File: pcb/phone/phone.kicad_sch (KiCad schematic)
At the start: 27 parts, among them CN1 S2B-PH-SM4-TB, U4 TPS63021DSJR, U5 TPS7A0218PDBVR, U6 MCP73831-2ACI/MC, U7 MAX17048G+T10

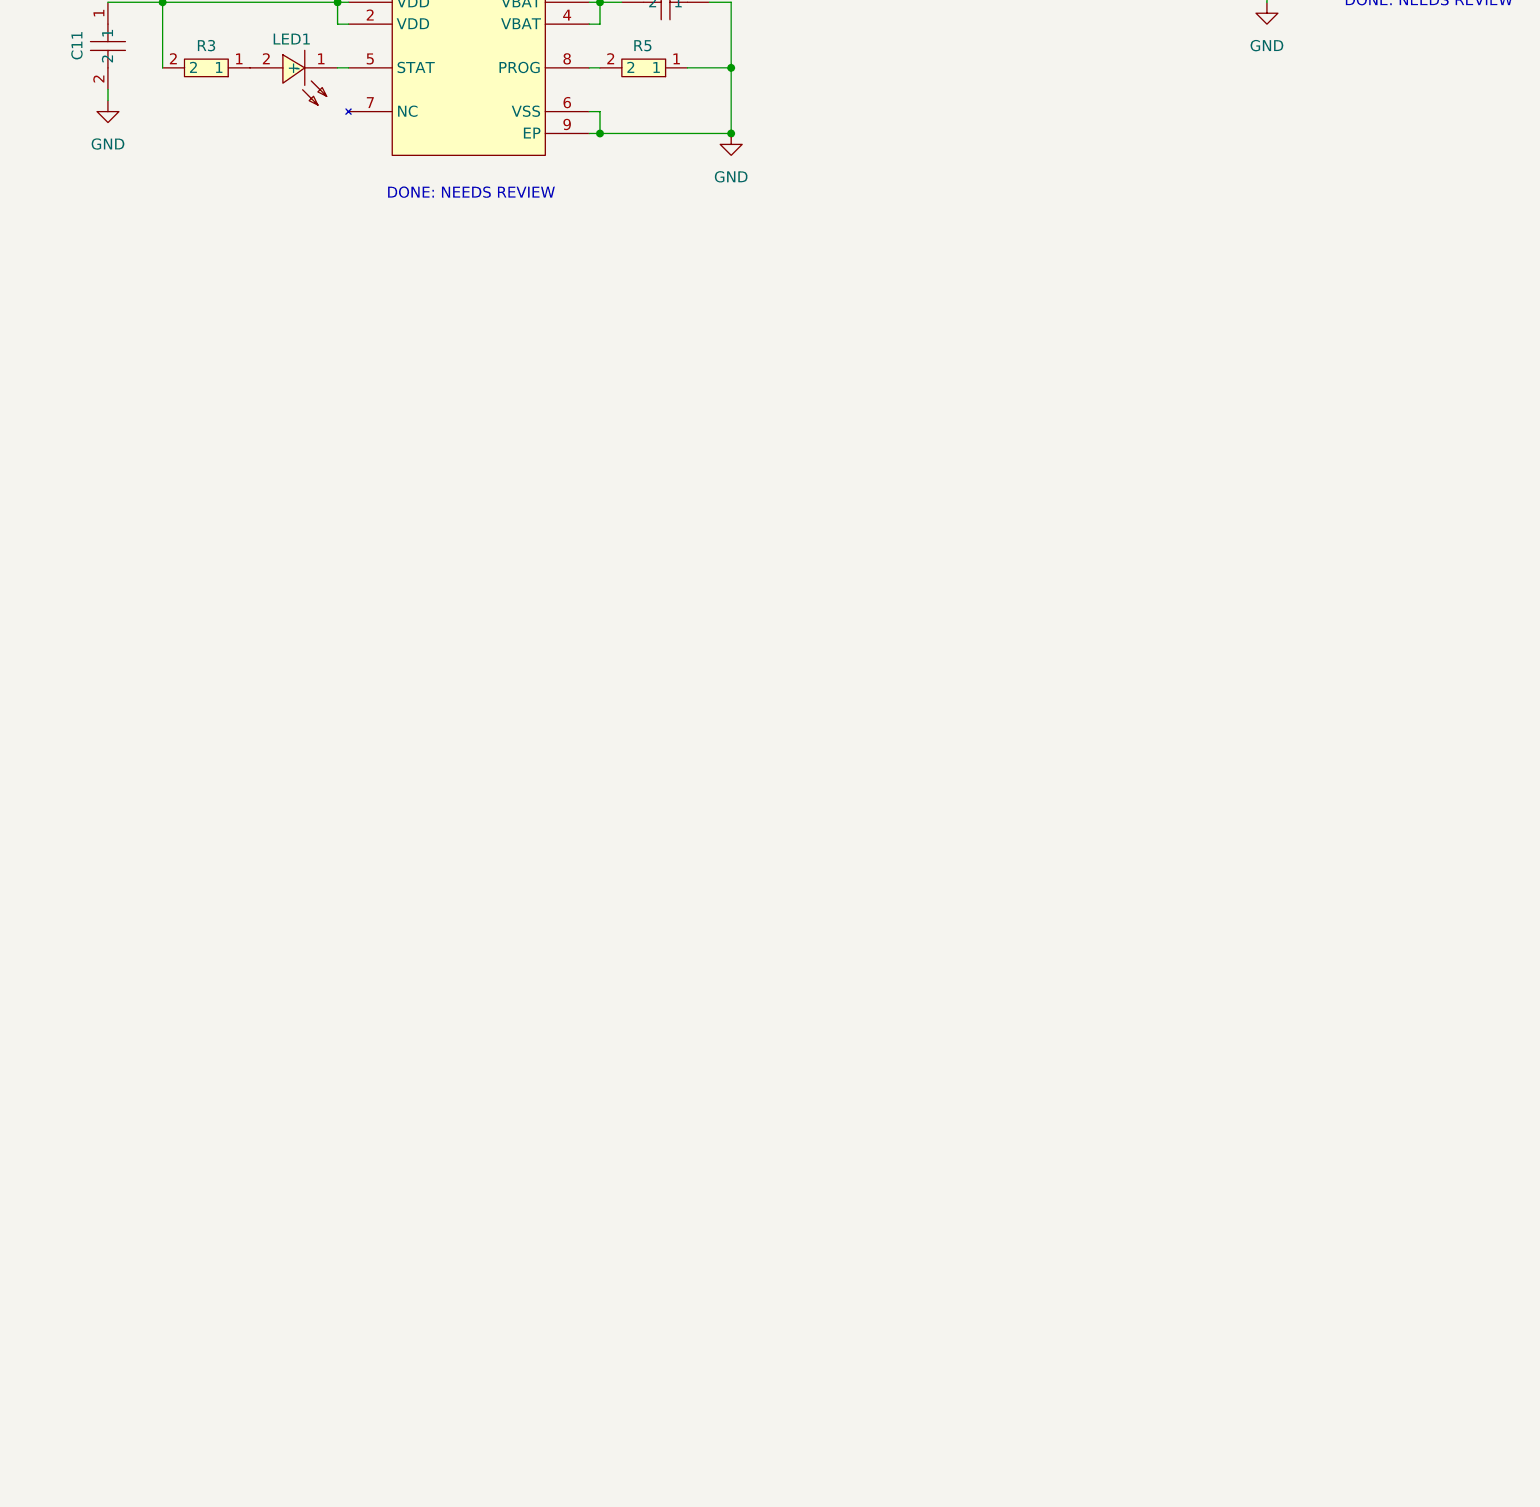
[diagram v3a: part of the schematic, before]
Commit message: Phase 3.2: Add MCU section (STM32H743ZIT6) to schematic
- Placed U1 (STM32H743ZIT6, LQFP-144) at (99.06, 248.92)
- 45 global labels on peripheral pins (UART, I2C, SPI, I2S2, SDMMC1,
  keypad, modem control, power monitoring, USB, SWD, backlight PWM)
- 67 no-connect markers on unused/spare pins
- 12x 100nF decoupling caps on VDD pins (C19-C30)
- 2x 2.2uF VCAP caps on pins 71/106 (C17, C18)
- 8MHz HSE crystal (Y1) + 2x 22pF load caps (C12, C13)
- NRST: 10kΩ pullup (R8) + 100nF cap (C16)
- BOOT0: 10kΩ pulldown (R9), PDR_ON: 10kΩ pullup (R10)
- 59 power symbols for +3.3V/GND connections
- ERC: 5 pre-existing power errors, 41 isolated-pin warnings (expected
  — external components not yet placed)
- Power section untouched (protected)

Pin assignment verified against docs/mcu-pin-assignment.md (DS12110 Rev 11)

Generated with [Devin](https://devin.ai)

Co-Authored-By: Devin <158243242+devin-ai-integration[bot]@users.noreply.github.com>
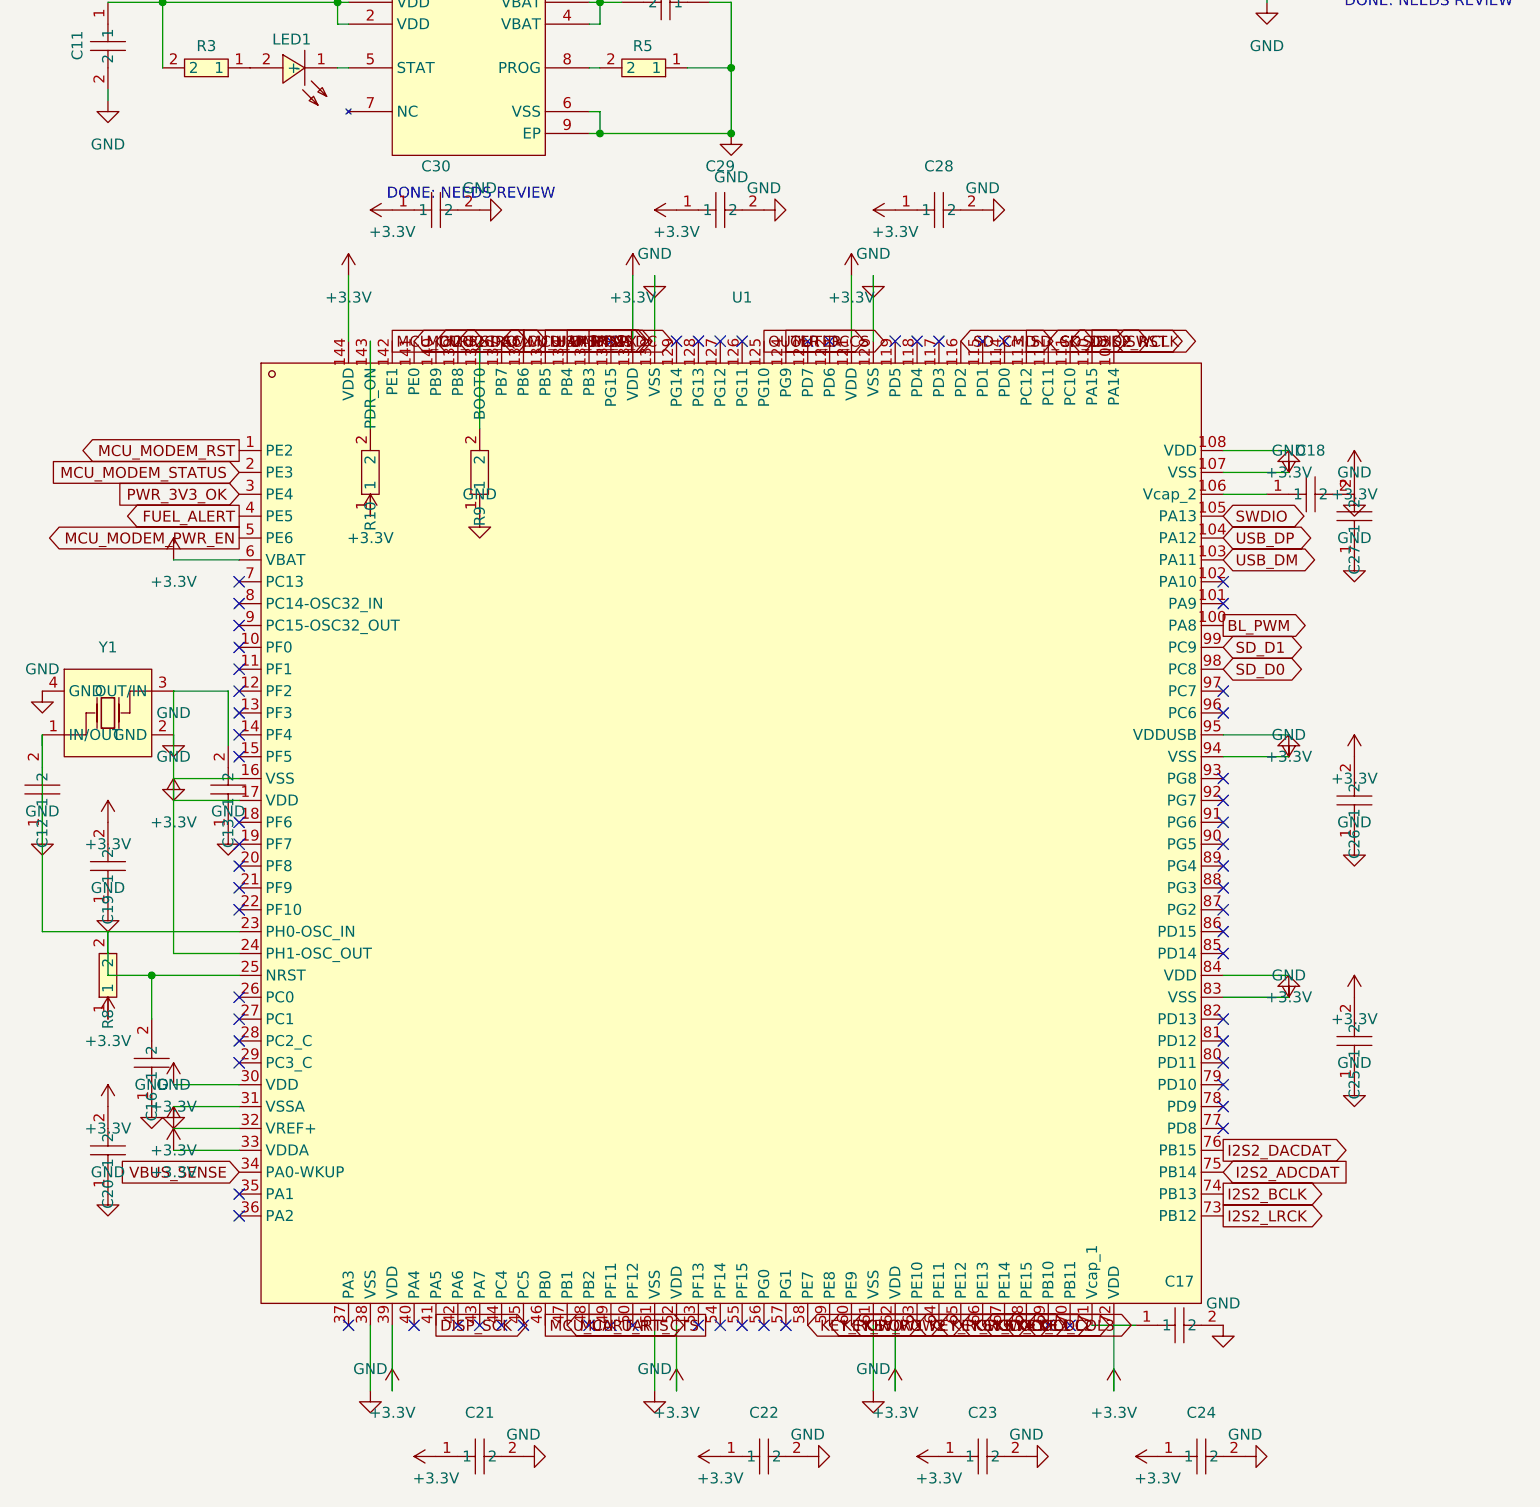
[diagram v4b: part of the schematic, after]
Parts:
- added C12, C13: 22pF, easyeda2kicad:C0603, symbol passives:CC0603KRX7R9BB104
- added C16, C19, C20, C21, C22, C23, C24, C25, C26, C27, C28, C29, C30: 100nF, easyeda2kicad:C0603, symbol passives:CC0603KRX7R9BB104
- added C17, C18: 2.2uF, easyeda2kicad:C0603, symbol passives:GRM188R61C475KE11D
- added R10, R8, R9: 10k, easyeda2kicad:C0603, symbol passives:RC0603JR-0710KL
- added U1: STM32H743ZIT6, easyeda2kicad:LQFP-144_L20.0-W20.0-P0.50-LS22.0-BL, symbol ics:STM32H743ZIT6
- added Y1: ECS-80-12-33Q-GN-TR, easyeda2kicad:CRYSTAL-SMD_4P-L3.2-W2.5-BL, symbol electromech:ECS-80-12-33Q-GN-TR
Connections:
- net +3.3V: now also C19.2, C20.2, C21.1, C22.1, C23.1, C24.1, C25.2, C26.2, C27.2, C28.1, C29.1, C30.1, R10.1, R8.1, U1.108 (VDD), U1.121 (VDD), U1.131 (VDD), U1.144 (VDD), U1.17 (VDD), U1.30 (VDD), U1.32 (VREF+), U1.33 (VDDA), U1.39 (VDD), U1.52 (VDD), U1.6 (VBAT), U1.62 (VDD), U1.72 (VDD), U1.84 (VDD), U1.95 (VDDUSB)
- net FUEL_ALERT: now also U1.4 (PE5)
- net GND: now also C12.1, C13.1, C16.1, C17.2, C18.2, C19.1, C20.1, C21.2, C22.2, C23.2, C24.2, C25.1, C26.1, C27.1, C28.2, C29.2, C30.2, R9.1, U1.107 (VSS), U1.120 (VSS), U1.130 (VSS), U1.16 (VSS), U1.31 (VSSA), U1.38 (VSS), U1.51 (VSS), U1.61 (VSS), U1.83 (VSS), U1.94 (VSS), Y1.2 (GND), Y1.4 (GND)
- net I2C_SCL: now also U1.139 (PB8)
- net I2C_SDA: now also U1.140 (PB9)
- net USB_DP: now also U1.104 (PA12)
- new net: R10.2, U1.143 (PDR_ON)
- new net: C16.2, R8.2, U1.25 (NRST)
- new net: C13.2, U1.24 (PH1-OSC_OUT), Y1.3 (OUT/IN)
- new net: C17.1, U1.71 (Vcap_1)
- new net: R9.2, U1.138 (BOOT0)
- new net: C12.2, U1.23 (PH0-OSC_IN), Y1.1 (IN/OUT)
- new net: C18.1, U1.106 (Vcap_2)
- new net BL_PWM: U1.100 (PA8)
- new net DISP_CS: U1.134 (PB4)
- new net DISP_DC: U1.133 (PB3)
- new net DISP_MOSI: U1.135 (PB5)
- new net DISP_RST: U1.110 (PA15)
- new net DISP_SCK: U1.41 (PA5)
- new net I2S2_ADCDAT: U1.75 (PB14)
- new net I2S2_BCLK: U1.74 (PB13)
- new net I2S2_DACDAT: U1.76 (PB15)
- new net I2S2_LRCK: U1.73 (PB12)
- new net KEY_COL0: U1.65 (PE12)
- new net KEY_COL1: U1.66 (PE13)
- new net KEY_COL2: U1.67 (PE14)
- new net KEY_COL3: U1.68 (PE15)
- new net KEY_ROW0: U1.58 (PE7)
- new net KEY_ROW1: U1.59 (PE8)
- new net KEY_ROW2: U1.60 (PE9)
- new net KEY_ROW3: U1.63 (PE10)
- new net KEY_ROW4: U1.64 (PE11)
- new net MCU_DTR: U1.142 (PE1)
- new net MCU_MODEM_PWR_EN: U1.5 (PE6)
- new net MCU_MODEM_RST: U1.1 (PE2)
- new net MCU_MODEM_STATUS: U1.2 (PE3)
- new net MCU_RI_IRQ: U1.141 (PE0)
- new net MCU_UART_CTS: U1.47 (PB1)
- new net MCU_UART_RTS: U1.46 (PB0)
- new net MCU_UART_RX: U1.137 (PB7)
- new net MCU_UART_TX: U1.136 (PB6)
- new net OUTER_CS: U1.124 (PG9)
- new net OUTER_DC: U1.125 (PG10)
- new net PWR_3V3_OK: U1.3 (PE4)
- new net SD_CK: U1.113 (PC12)
- new net SD_CMD: U1.116 (PD2)
- new net SD_D0: U1.98 (PC8)
- new net SD_D1: U1.99 (PC9)
- new net SD_D2: U1.111 (PC10)
- new net SD_D3: U1.112 (PC11)
- new net SWCLK: U1.109 (PA14)
- new net SWDIO: U1.105 (PA13)
- new net USB_DM: U1.103 (PA11)
- new net VBUS_SENSE: U1.34 (PA0-WKUP)
- no-connect marks 0 -> 67
